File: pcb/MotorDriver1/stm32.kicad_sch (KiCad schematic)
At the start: 29 parts, among them IC1 STM32C092RCT6, J1 GT-USB-7010ASV, SW1 K2-6639SP-C4SC-04, SW2 K2-6639SP-C4SC-04, SW3 K2-6639SP-C4SC-04, U1 NCP361SNT1G, U2 CH340X, Y1 48 MHz, Y2 32.768 kHz

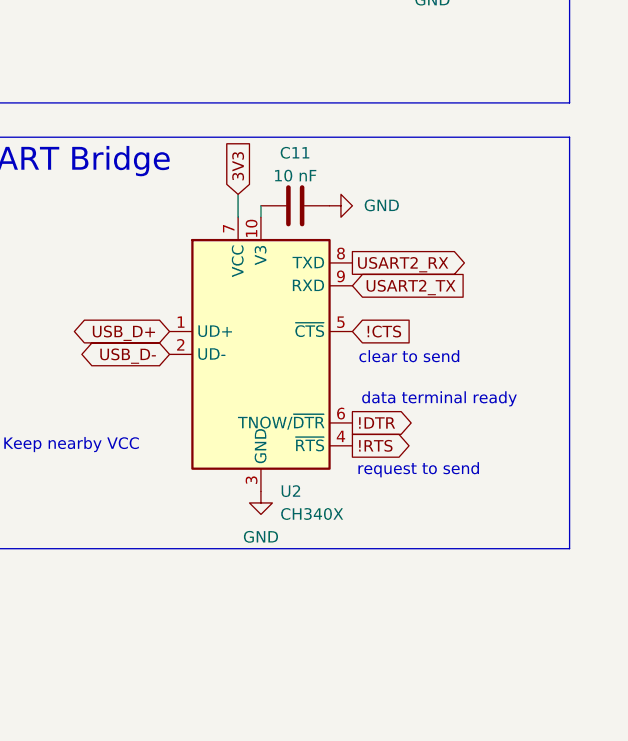
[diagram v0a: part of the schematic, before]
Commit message: Modifying usb uart schematic
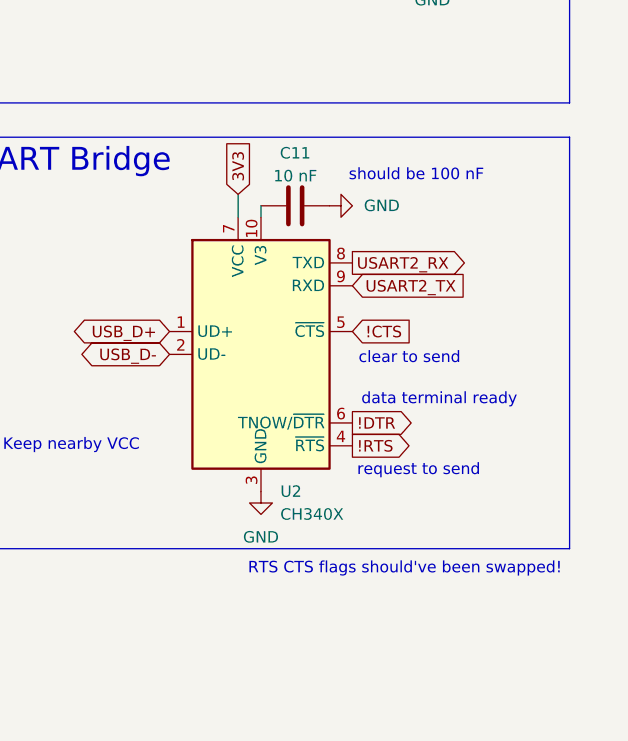
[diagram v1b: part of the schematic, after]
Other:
- note added: "RTS CTS flags should've been swapped!"
- note added: "should be 100 nF"
